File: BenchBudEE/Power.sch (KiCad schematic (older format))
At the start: 11 parts, among them P1 CONN_12X2, SW1 SWITCH_INV

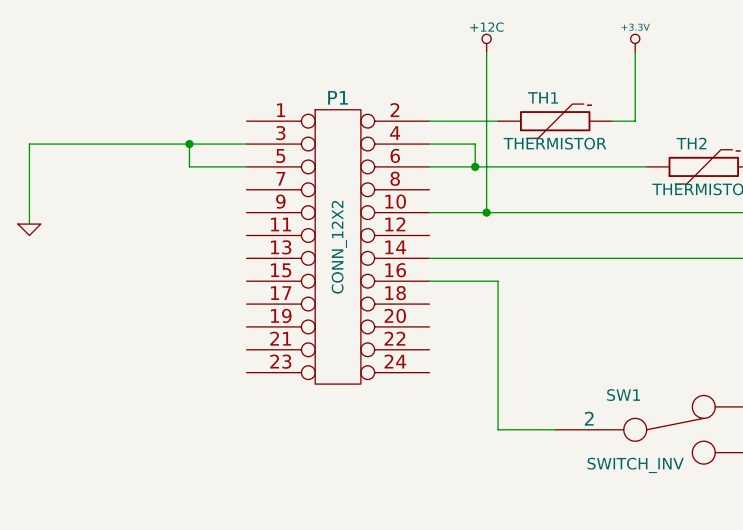
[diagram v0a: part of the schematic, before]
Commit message: Arduino module associated + roughly placed.
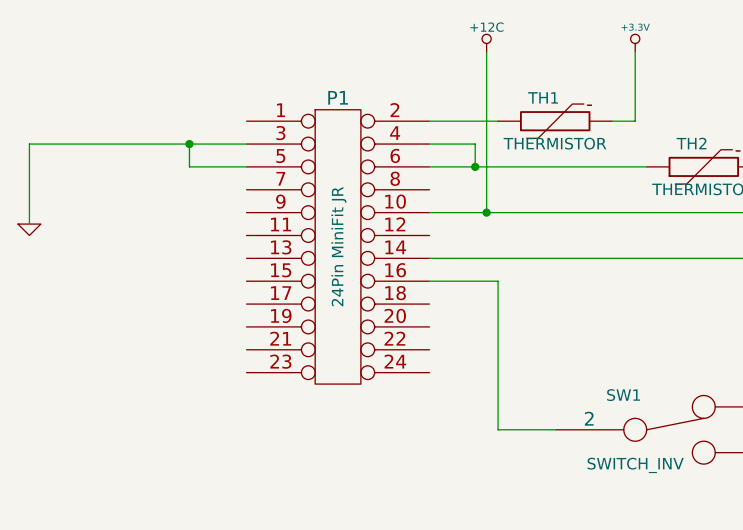
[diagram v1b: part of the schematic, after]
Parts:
- P1: value CONN_12X2 -> 24Pin MiniFit JR; Distributor (none) -> Mouser; Distributor Part Link (none) -> http://uk.mouser.com/ProductDetail/Molex/39-30-1240/?qs=sGA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; Distributor Part Number (none) -> 538-39-30-1240; MFG Name (none) -> Molex; MFG Part Number (none) -> 39-30-1240
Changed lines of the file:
@@
 Sheet 5 9
 Title ""
-Date "20 feb 2014"
+Date "23 feb 2014"
 Rev ""
 Comp ""
@@
 P 3000 2300
 F 0 "P1" H 3000 2950 60  0000 C CNN
-F 1 "CONN_12X2" V 3000 2300 50  0000 C CNN
+F 1 "24Pin MiniFit JR" V 3000 2300 50  0000 C CNN
 F 2 "" H 3000 2300 60  0000 C CNN
-F 3 "" H 3000 2300 60  0000 C CNN
+F 3 "http://www.molex.com/webdocs/datasheets/pdf/en-us/0039301240_PCB_HEADERS.pdf" H 3000 2300 60  0001 C CNN
+F 4 "Molex" H 3000 2300 60  0001 C CNN "MFG Name"
+F 5 "39-30-1240" H 3000 2300 60  0001 C CNN "MFG Part Number"
+F 6 "Mouser" H 3000 2300 60  0001 C CNN "Distributor"
+F 7 "538-39-30-1240" H 3000 2300 60  0001 C CNN "Distributor Part Number"
+F 8 "http://uk.mouser.com/ProductDetail/Molex/39-30-1240/?qs=sGAEpiMZZMs%252bGHln7q6pm%252bS0pk2Wo0Xxrf8ldfSZpwQ=" H 3000 2300 60  0001 C CNN "Distributor Part Link"
 	1    3000 2300
 	1    0    0    -1

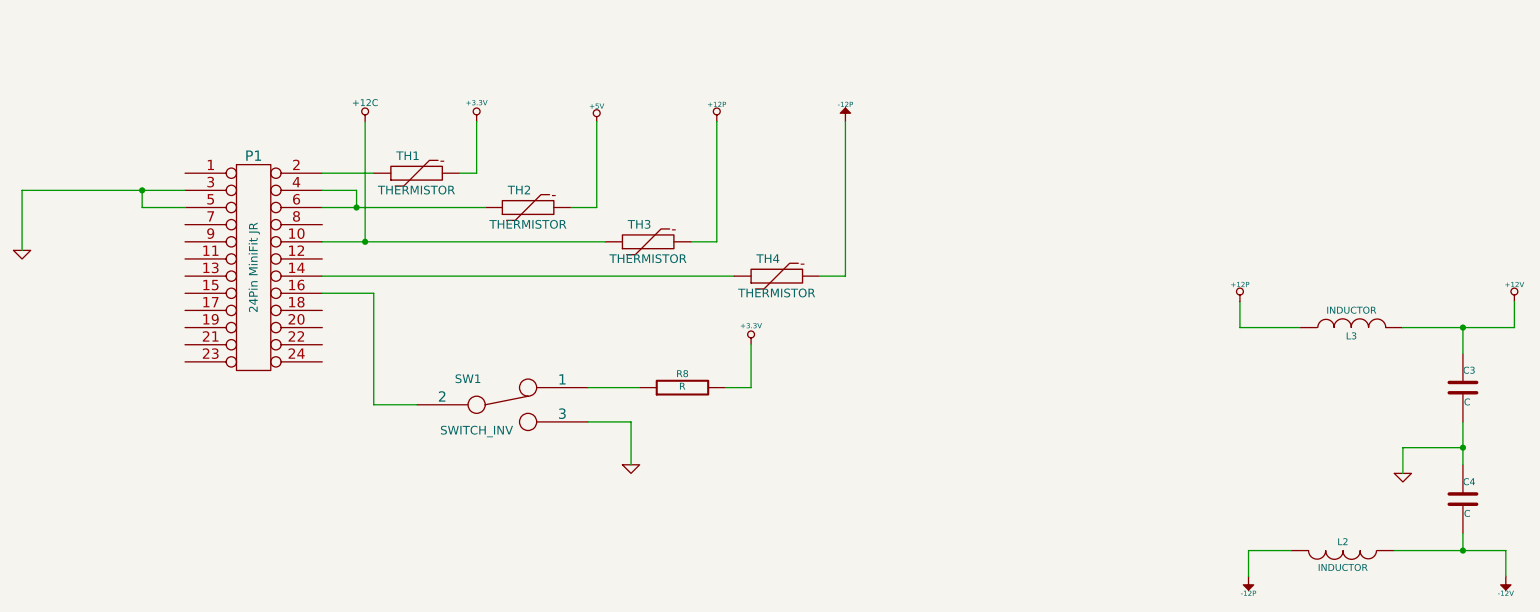
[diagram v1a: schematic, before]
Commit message: Power Module associated + roughly placed.
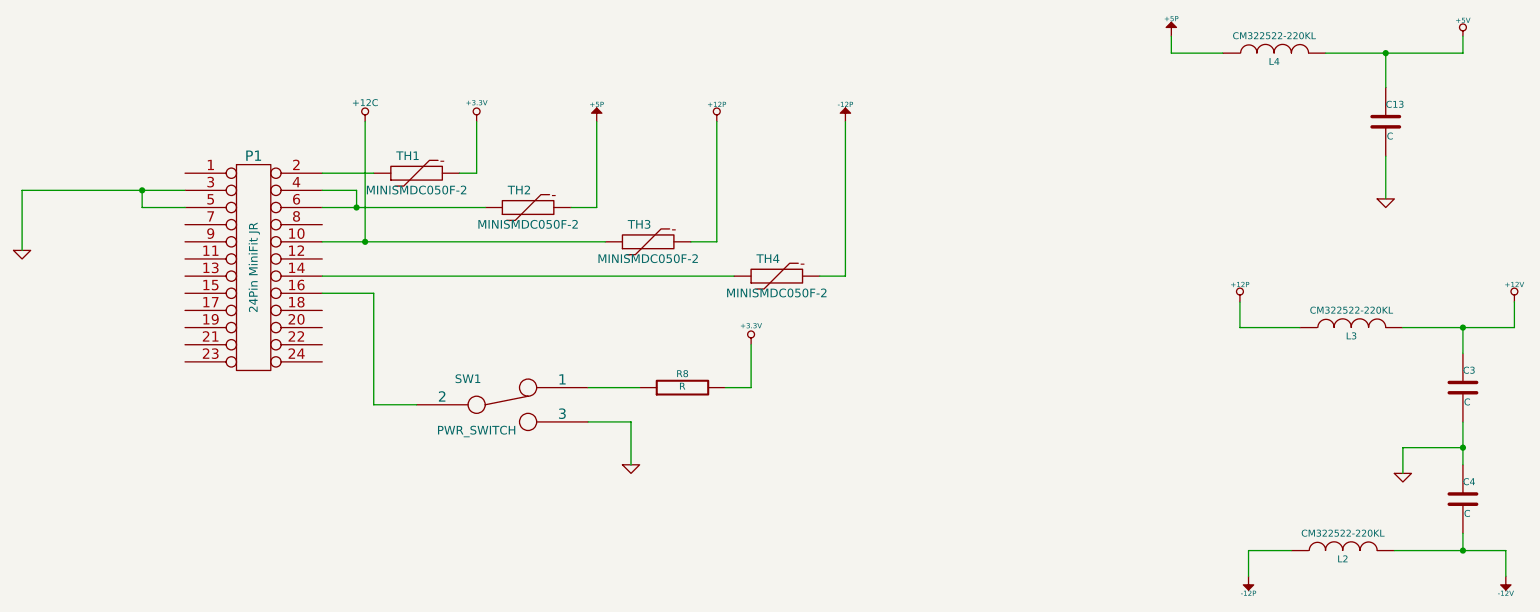
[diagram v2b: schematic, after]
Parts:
- added C13: C, ~, symbol C
- added L4: CM322522-220KL, ~, symbol INDUCTOR
- L2, L3: value INDUCTOR -> CM322522-220KL; Distributor (none) -> DigiKey; Distributor Part Link (none) -> http://www.digikey.com/product-detail/en/CM322522-220KL/CM3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; Distributor Part Number (none) -> CM322522-220KLCT-ND; MFG Name (none) -> Bourns Inc.; MFG Part Number (none) -> CM322522-220KL
- SW1: value SWITCH_INV -> PWR_SWITCH; Distributor (none) -> DigiKey; Distributor Part Link (none) -> www.digikey.com/product-detail/en/OS102011MA1QN1/CKN9559-ND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; Distributor Part Number (none) -> CKN9559-ND; MFG Name (none) -> C&K Components; MFG Part Number (none) -> OS102011MA1QN1
- TH1, TH2, TH3, TH4: value THERMISTOR -> MINISMDC050F-2; Distributor (none) -> DigiKey; Distributor Part Link (none) -> http://www.digikey.com/product-detail/en/MINISMDC050F-2/MIN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; Distributor Part Number (none) -> MINISMDC050FCT-ND; MFG Name (none) -> TE Connectivity; MFG Part Number (none) -> MINISMDC050F-2
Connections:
- net +5V: now also C13.1, L4.2; no longer TH2.2
- net -12P: now also L2.1; no longer L2.2
- net -12V: now also L2.2; no longer L2.1
- net GND: now also C13.2
- new net +5P: L4.1, TH2.2
